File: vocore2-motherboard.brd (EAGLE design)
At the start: 100 x 100 mm, 104 parts, among them IC1 AP63205, IC2 FE1.1S, IC3 LM3671MF-3.3, IC4 LM3671MF-3.3, IC5 LM3671MF-3.3, IC7 742G17DBV, IC8 FT230XS-R, J1 RJHSE-5381, J2 TE_1775470-8, J3 AMPHENOL_1140084168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

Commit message: feat(pcb): Beschriftung Phoenix Stromstecker
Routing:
- net GND: vias 331 -> 328
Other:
- board text added: "24V"
- board text added: "PE"
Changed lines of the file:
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@@
 <layer number="24" name="bOrigins" color="15" fill="1" visible="yes" active="yes"/>
 <layer number="25" name="tNames" color="7" fill="1" visible="yes" active="yes"/>
-<layer number="26" name="bNames" color="7" fill="1" visible="no" active="yes"/>
+<layer number="26" name="bNames" color="7" fill="1" visible="yes" active="yes"/>
 <layer number="27" name="tValues" color="7" fill="1" visible="yes" active="yes"/>
 <layer number="28" name="bValues" color="7" fill="1" visible="yes" active="yes"/>
@@
 <text x="-3.7" y="12.9" size="1.1" layer="25" align="bottom-center">VUSB</text>
 <rectangle x1="9.5" y1="7.15" x2="50" y2="32.15" layer="157"/>
+<text x="-31.2" y="1.7" size="1.2" layer="26" rot="MR0" align="bottom-center">24V</text>
+<text x="-35" y="1.8" size="1.2" layer="26" rot="MR0" align="bottom-center">GND</text>
+<text x="-38.8" y="1.8" size="1.2" layer="26" rot="MR0" align="bottom-center">PE</text>
 </plain>
 <attributes>
@@
 <contactref element="C18" pad="2"/>
 <contactref element="D1" pad="A"/>
-<via x="-36.7" y="2.3" extent="1-16" drill="0.31"/>
-<via x="-36" y="2.3" extent="1-16" drill="0.31"/>
-<via x="-35.3" y="2.3" extent="1-16" drill="0.31"/>
-<via x="-34.6" y="2.3" extent="1-16" drill="0.31"/>
-<via x="-33.9" y="2.3" extent="1-16" drill="0.31"/>
-<via x="-33.2" y="2.3" extent="1-16" drill="0.31"/>
-<via x="-36.7" y="1.6" extent="1-16" drill="0.31"/>
-<via x="-36" y="1.6" extent="1-16" drill="0.31"/>
-<via x="-35.3" y="1.6" extent="1-16" drill="0.31"/>
-<via x="-34.6" y="1.6" extent="1-16" drill="0.31"/>
-<via x="-33.9" y="1.6" extent="1-16" drill="0.31"/>
-<via x="-33.2" y="1.6" extent="1-16" drill="0.31"/>
 <contactref element="IC2" pad="1"/>
 <contactref element="C3" pad="2"/>
@@
 <via x="-22.5" y="46.5" extent="1-16" drill="0.35"/>
 <via x="23" y="46.6" extent="1-16" drill="0.35"/>
+<via x="39.3" y="34.8" extent="1-16" drill="0.35"/>
+<via x="39.3" y="33.7" extent="1-16" drill="0.35"/>
+<via x="40.7" y="33.7" extent="1-16" drill="0.35"/>
+<via x="40.7" y="34.8" extent="1-16" drill="0.35"/>
+<via x="45.6" y="34.9" extent="1-16" drill="0.35"/>
+<via x="45.6" y="33.7" extent="1-16" drill="0.35"/>
+<via x="46.9" y="34.9" extent="1-16" drill="0.35"/>
+<via x="46.9" y="33.7" extent="1-16" drill="0.35"/>
+<via x="46.9" y="36.1" extent="1-16" drill="0.35"/>
 </signal>
 <signal name="N$1">

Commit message: feat: TVS diodes on MiniPCIe slots
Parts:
- added D5, D6, D7: PRTR5V0U2X, diode:SOT143
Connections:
- net GND: now also D5.1, D6.1, D7.1
- net X1_3V3: now also D7.4
- net X1_USB_D+: now also D7.3
- net X1_USB_D-: now also D7.2
- net X2_3V3: now also D6.4
- net X2_USB_D+: now also D6.3
- net X2_USB_D-: now also D6.2
- net X3_3V3: now also D5.4
- net X3_USB_D+: now also D5.3
- net X3_USB_D-: now also D5.2
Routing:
- net X2_USB_D+: track 39.5 -> 43.3 mm
- net X3_USB_D+: track 48.6 -> 52.5 mm
- net X3_USB_D-: track 50.4 -> 54.1 mm
- net X2_USB_D-: track 40.8 -> 44.4 mm
- net X1_USB_D+: track 73.2 -> 76.3 mm
- net X3_3V3: track 62.5 -> 65.5 mm
- net X1_USB_D-: track 74.6 -> 77.4 mm
- net X2_3V3: track 63.4 -> 65.8 mm
- net X1_3V3: track 62.9 -> 65.3 mm
- net GND: vias 328 -> 325

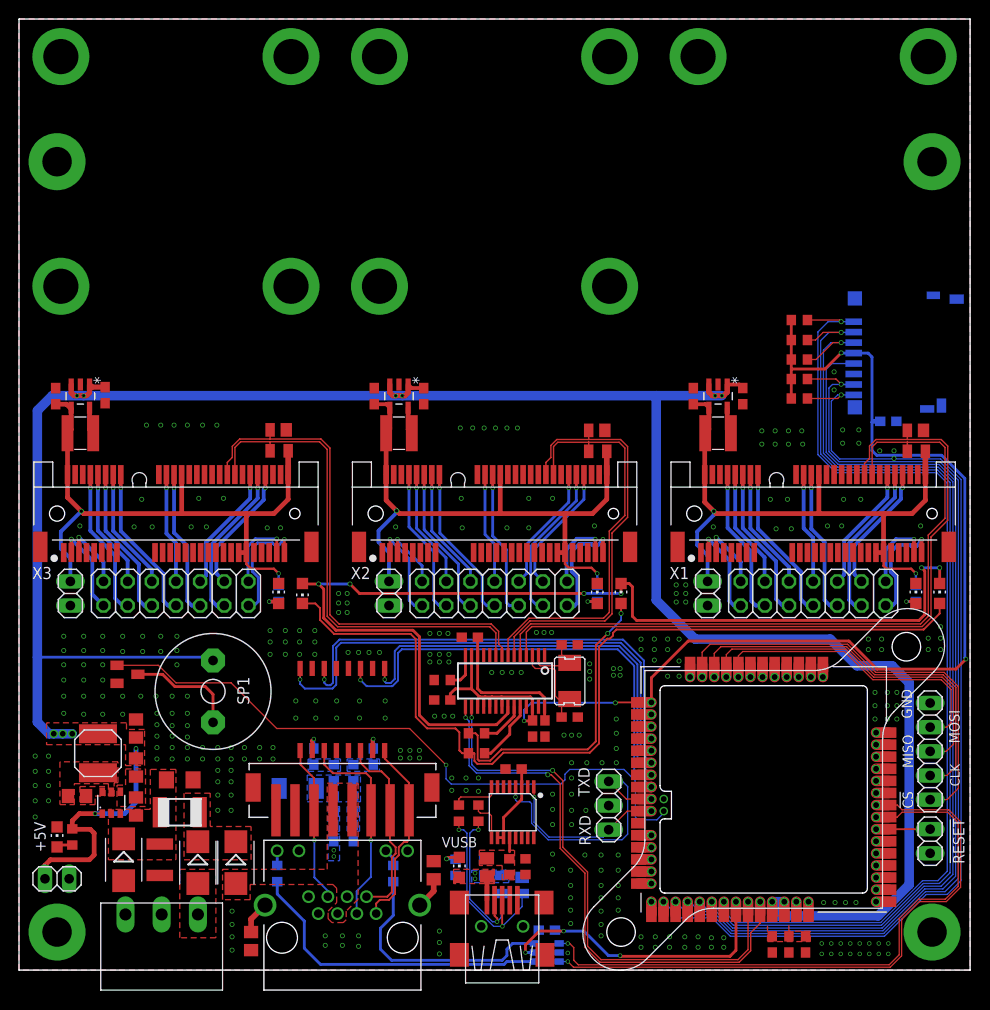
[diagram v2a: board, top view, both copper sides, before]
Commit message: feat: network led breakout
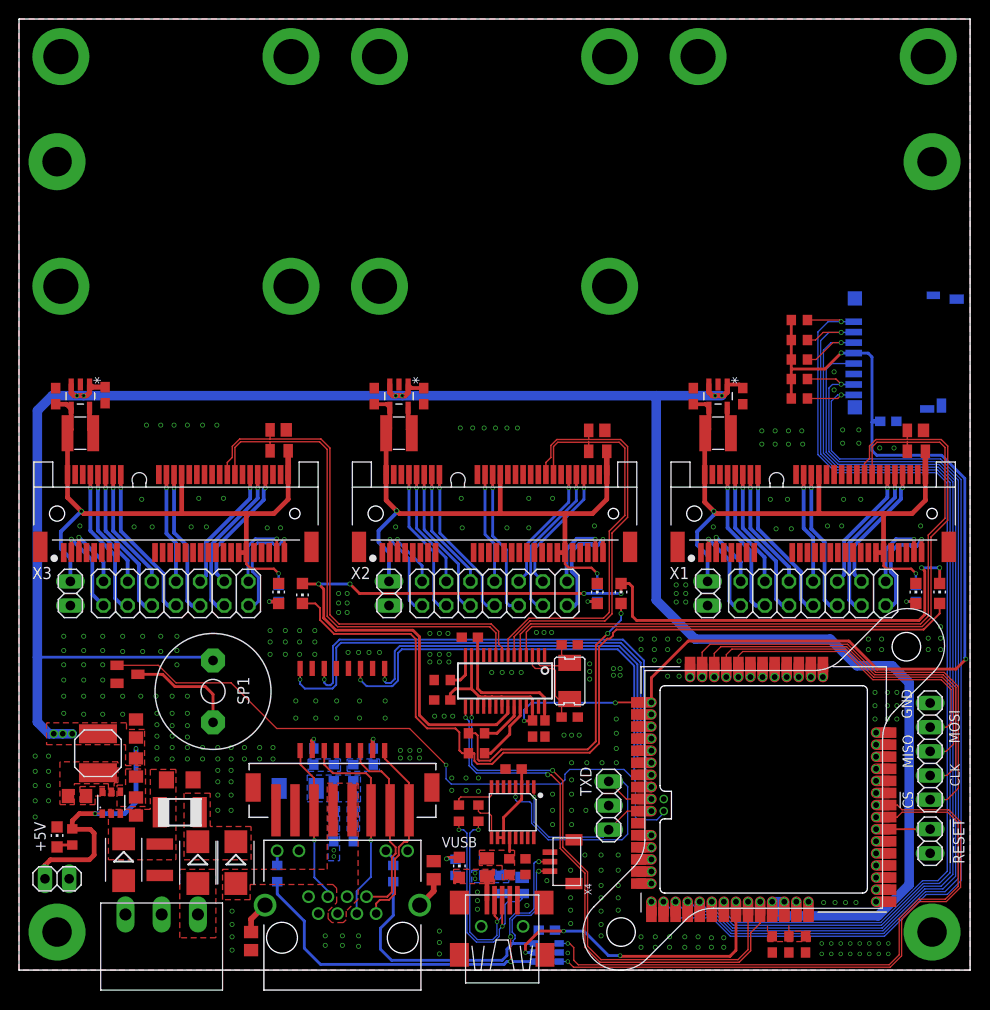
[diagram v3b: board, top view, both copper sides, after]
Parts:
- added X4: BM03B-SRSS-TB, con-jst:BM03B-SRSS-TB
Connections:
- net GND: now also X4.3, X4.G1, X4.G2
- net N$37: now also X4.2
- net N$66: now also X4.1
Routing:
- net N$37: track 33.2 -> 47.3 mm, vias 0 -> 3
- net N$66: track 25.5 -> 36.6 mm, vias 0 -> 1
- net USB_D+: track 20.9 -> 25.4 mm
- net USB_D-: track 18.3 -> 22.7 mm
- net GND: vias 325 -> 326
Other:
- board text removed: "RXD"

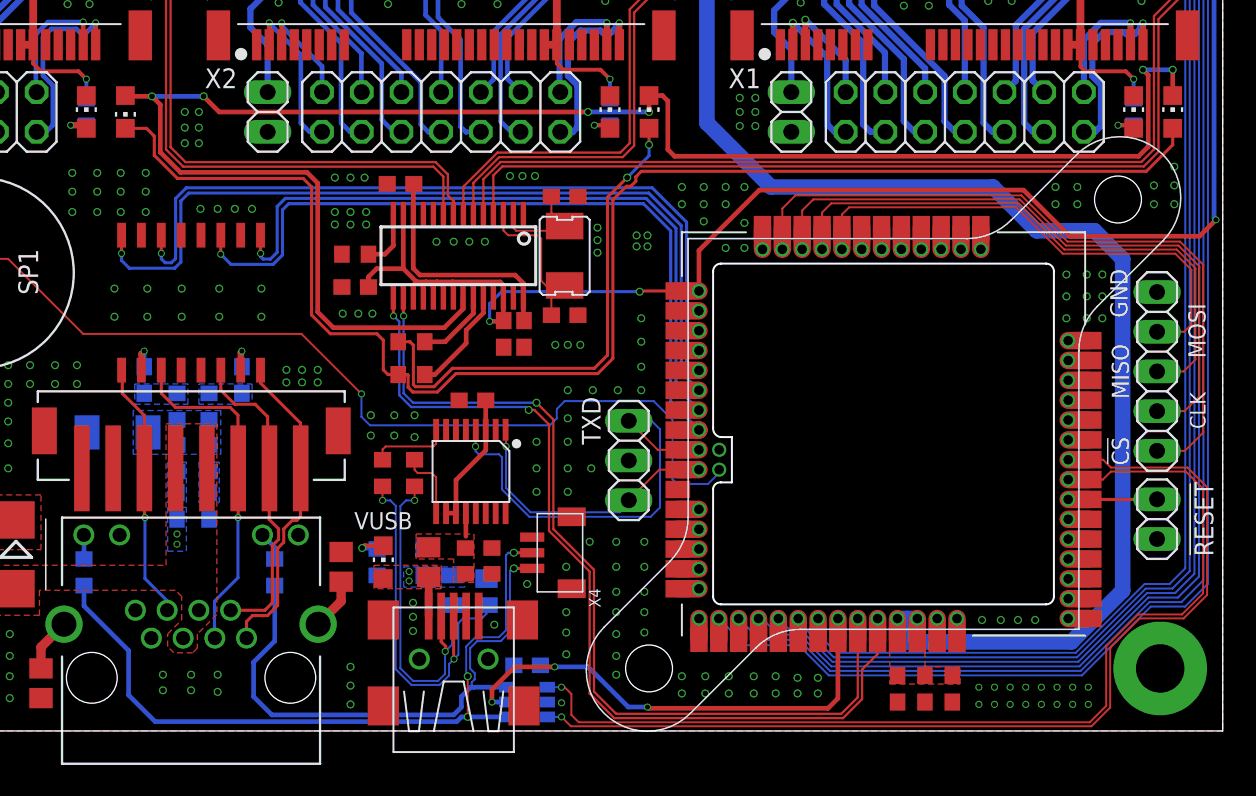
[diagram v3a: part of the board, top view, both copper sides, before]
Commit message: feat(pcb): removed through-hole mounts for vocore2
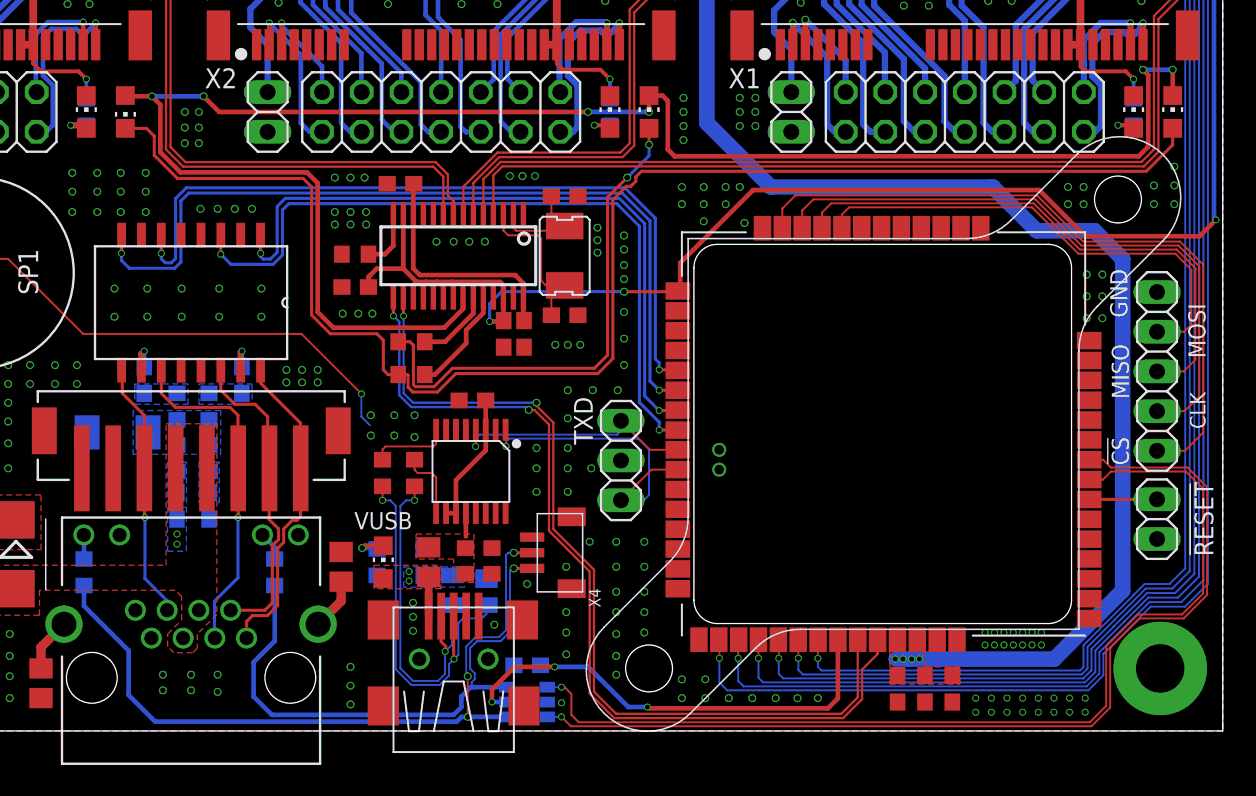
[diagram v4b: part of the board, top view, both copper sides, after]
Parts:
- LED8: value RED -> GREEN
- R3: value 330R -> 470R
- moved JP4 0.50 mm to (11.5, 17.3)
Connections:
- net !VC_RESET: no longer U1.138_1
- net +5V: no longer U1.+5.0V_1, U1.+5.0V_2
- net GND: no longer U1.GND1, U1.GND2, U1.GND3, U1.GND4, U1.GND5, U1.GND6, U1.GND7
- net LED_LAN_ACT: no longer U1.143_1
- net LED_LAN_LNK: no longer U1.142_1
- net N$19: no longer U1.24_1
- net N$23: no longer U1.148_1
- net N$24: no longer U1.147_1
- net N$25: no longer U1.30_1
- net N$26: no longer U1.31_1
- net N$27: no longer U1.29_1
- net N$30: no longer U1.46_1
- net N$31: no longer U1.47_1
- net N$32: no longer U1.48_1
- net N$34: no longer U1.136_1
- net N$35165: no longer U1.137_1
- net N$43: no longer U1.139_1
- net N$44: no longer U1.140_1
- net N$45: no longer U1.141_1
- net N$48: no longer U1.+1.8V_1
- net N$49: no longer U1.18_1
- net N$51: no longer U1.19_1
- net N$52: no longer U1.17_1
- net N$53: no longer U1.16_1
- net N$54: no longer U1.20_1
- net N$55: no longer U1.21_1
- net P0_RD+: no longer U1.33_1
- net P0_RD-: no longer U1.34_1
- net P0_TD+: no longer U1.35_1
- net P0_TD-: no longer U1.36_1
- net USB_UP_D+: no longer U1.61_1
- net USB_UP_D-: no longer U1.62_1
- net VC_3V3: no longer U1.+3.3V_1, U1.+3.3V_2, U1.+3.3V_3
- net VC_SD_CD: no longer U1.50_1
- net VC_SD_CLK: no longer U1.54_1
- net VC_SD_CMD: no longer U1.55_1
- net VC_SD_D0: no longer U1.52_1
- net VC_SD_D1: no longer U1.51_1
- net VC_SD_D2: no longer U1.57_1
- net VC_SD_D3: no longer U1.56_1
- net VC_SD_WP: no longer U1.49_1
- net VC_SPI_CLK: no longer U1.25_1
- net VC_SPI_CS0: no longer U1.28_1
- net VC_SPI_MISO: no longer U1.26_1
- net VC_SPI_MOSI: no longer U1.27_1
- net VOCORE_RXD2: no longer U1.44_1
- net VOCORE_TXD2: no longer U1.43_1
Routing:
- net VC_PWM1: track 69.4 -> 41.2 mm
- net VOCORE_TXD2: track 28.9 -> 16.1 mm
- net GND: track 9.44 -> 0.00 mm, vias 326 -> 329
- net +5V: track 270.0 -> 262.1 mm, vias 11 -> 15
- net VC_3V3: track 167.8 -> 163.4 mm
- net LED_LAN_LNK: track 66.7 -> 64.0 mm
- net VC_SPI_MOSI: track 33.7 -> 31.0 mm
- net VC_SPI_CS0: track 47.2 -> 44.6 mm
- net VC_SPI_CLK: track 42.7 -> 40.0 mm
- net P0_RD+: track 51.9 -> 49.3 mm, vias 1 -> 2
- net VC_SPI_MISO: track 38.2 -> 35.8 mm
- net VOCORE_RXD2: track 18.0 -> 20.2 mm
- net P0_RD-: track 55.1 -> 52.9 mm, vias 1 -> 2
- net P0_TD-: track 49.1 -> 46.9 mm, vias 1 -> 2
- net P0_TD+: track 45.7 -> 43.6 mm, vias 1 -> 2
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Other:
- outline, holes or cut-outs redrawn
